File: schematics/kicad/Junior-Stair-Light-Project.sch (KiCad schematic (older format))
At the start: 107 parts, among them J1 12V Eingang, J3 CONN_01X03, J4 CONN_01X03, J5 Conn_01x10, J6 Conn_01x10, T10_1 BC337, T10_2 BC327, T11_1 BC337, T11_2 BC327, T12_1 BC337, T12_2 BC327, T13_1 BC337, T13_2 BC327, T14_1 BC337, T14_2 BC327, T15_1 BC337, T15_2 BC327, T16_1 BC337, T16_2 BC327, T17_1 BC337, T17_2 BC327, T18_1 BC337, T18_2 BC327, T19_1 BC337, T19_2 BC327, T1_1 BC337, T1_2 BC327, T2_1 BC337, T2_2 BC327, T3_1 BC337, T3_2 BC327, T4_1 BC337, T4_2 BC327, T5_1 BC337, T5_2 BC327, T6_1 BC337, T6_2 BC327, T7_1 BC337, T7_2 BC327, T8_1 BC337, T8_2 BC327, T9_1 BC337, T9_2 BC327, U1 L4940V5, U2 Arduino_Nano

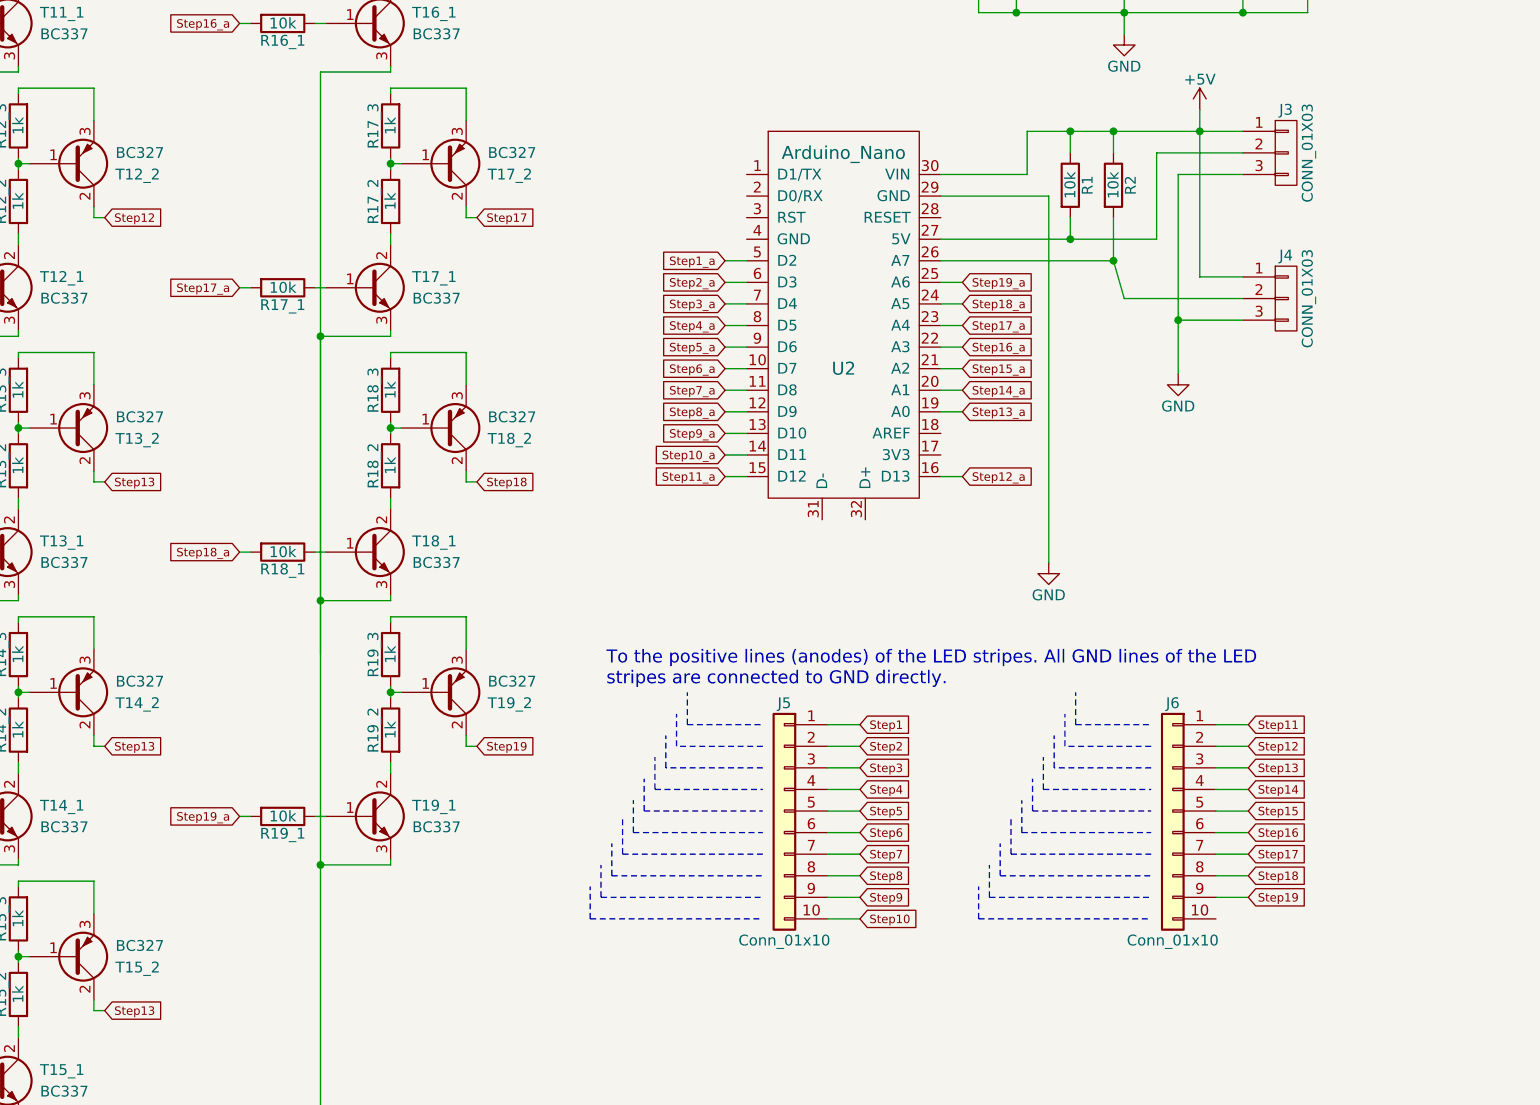
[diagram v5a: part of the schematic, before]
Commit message: Corrected connectivity, there was a bug
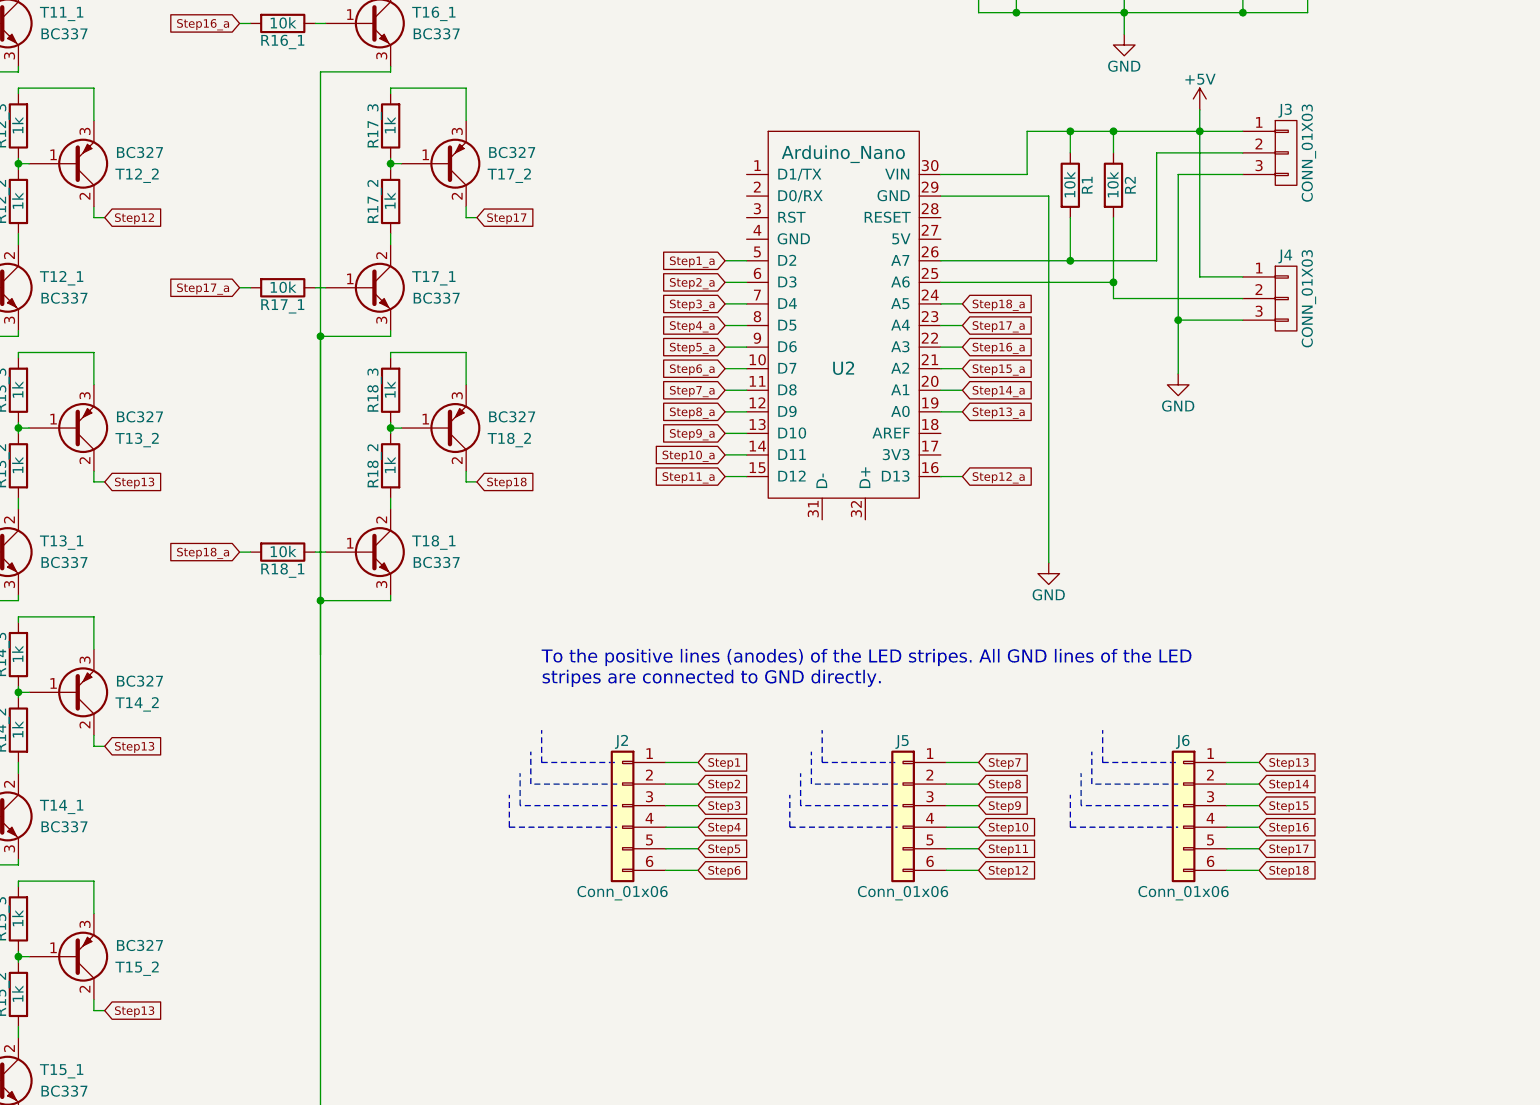
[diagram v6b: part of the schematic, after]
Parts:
- removed J5, J6: Conn_01x10, Connectors_JST:JST_XH_B10B-XH-A_10x2.50mm_Straight, symbol Conn_01x10
- removed R19_1: 10k, Resistors_THT:R_Axial_DIN0207_L6.3mm_D2.5mm_P7.62mm_Horizontal, symbol R
- removed R19_2, R19_3: 1k, Resistors_THT:R_Axial_DIN0207_L6.3mm_D2.5mm_P7.62mm_Horizontal, symbol R
- removed T19_1: BC337, TO_SOT_Packages_THT:TO-92_Inline_Narrow_Oval, symbol Q_NPN_BCE
- removed T19_2: BC327, TO_SOT_Packages_THT:TO-92_Inline_Narrow_Oval, symbol Q_PNP_BCE
- added J2, J5, J6: Conn_01x06, Connectors_JST:JST_XH_B06B-XH-A_06x2.50mm_Straight, symbol Conn_01x06
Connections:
- net Step19_a is gone; now on an unnamed net: U2.25 (A6)
- net Step1: now also J2.1 (Pin_1)
- net Step10: now also J5.4 (Pin_4)
- net Step11: now also J5.5 (Pin_5)
- net Step12: now also J5.6 (Pin_6)
- net Step13: now also J6.1 (Pin_1)
- net Step14: now also J6.2 (Pin_2)
- net Step15: now also J6.3 (Pin_3)
- net Step16: now also J6.4 (Pin_4)
- net Step17: now also J6.5 (Pin_5)
- net Step18: now also J6.6 (Pin_6)
- net Step2: now also J2.2 (Pin_2)
- net Step3: now also J2.3 (Pin_3)
- net Step4: now also J2.4 (Pin_4)
- net Step5: now also J2.5 (Pin_5)
- net Step6: now also J2.6 (Pin_6)
- net Step7: now also J5.1 (Pin_1)
- net Step8: now also J5.2 (Pin_2)
- net Step9: now also J5.3 (Pin_3)
- net at J4.2 (P2), R2.2: no longer U2.26 (A7)
- net at J3.2 (P2), R1.2: now also U2.26 (A7); no longer U2.27 (5V)

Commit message: Updates, updates, updates
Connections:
- net +5V: no longer R1.1, R2.1
- net GND: now also R1.1, R2.1
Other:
- moved on the sheet: R1, R2
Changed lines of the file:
@@
 L R R1
 U 1 1 5B89507E
-P 9825 2400
-F 0 "R1" V 9905 2400 50  0000 C CNN
-F 1 "10k" V 9825 2400 50  0000 C CNN
-F 2 "Resistors_THT:R_Axial_DIN0207_L6.3mm_D2.5mm_P7.62mm_Horizontal" V 9755 2400 50  0001 C CNN
-F 3 "" H 9825 2400 50  0001 C CNN
-	1    9825 2400
+P 9825 2550
+F 0 "R1" V 9905 2550 50  0000 C CNN
+F 1 "10k" V 9825 2550 50  0000 C CNN
+F 2 "Resistors_THT:R_Axial_DIN0207_L6.3mm_D2.5mm_P7.62mm_Horizontal" V 9755 2550 50  0001 C CNN
+F 3 "" H 9825 2550 50  0001 C CNN
+	1    9825 2550
 	1    0    0    -1
 $EndComp
@@
 	10325 2350 10325 3275
 Wire Wire Line
-	10625 2350 10325 2350
+	9825 2350 10625 2350
 Connection ~ 10325 3025
 $Comp
@@
 Connection ~ 10425 2150
 Wire Wire Line
-	10025 2550 10025 2925
+	10025 2700 10025 2925
 Wire Wire Line
 	10625 2250 10225 2250
@@
 L R R2
 U 1 1 5B89A934
-P 10025 2400
-F 0 "R2" V 10105 2400 50  0000 C CNN
-F 1 "10k" V 10025 2400 50  0000 C CNN
-F 2 "Resistors_THT:R_Axial_DIN0207_L6.3mm_D2.5mm_P7.62mm_Horizontal" V 9955 2400 50  0001 C CNN
-F 3 "" H 10025 2400 50  0001 C CNN
-	1    10025 2400
-	1    0    0    -1
-$EndComp
-Wire Wire Line
-	9825 2550 9825 2750
+P 10025 2550
+F 0 "R2" V 10105 2550 50  0000 C CNN
+F 1 "10k" V 10025 2550 50  0000 C CNN
+F 2 "Resistors_THT:R_Axial_DIN0207_L6.3mm_D2.5mm_P7.62mm_Horizontal" V 9955 2550 50  0001 C CNN
+F 3 "" H 10025 2550 50  0001 C CNN
+	1    10025 2550
+	1    0    0    -1
+$EndComp
+Wire Wire Line
+	9825 2700 9825 2750
 Connection ~ 9825 2750
 Connection ~ 10025 2850
@@
 	9400 1050 9400 1600
 Connection ~ 9575 1600
-Connection ~ 10025 2150
-Connection ~ 9825 2150
 Wire Wire Line
 	9625 2350 9625 2150
-Wire Wire Line
-	9825 2150 9825 2250
-Wire Wire Line
-	10025 2150 10025 2250
 Text GLabel 5975 1650 0    39   Input ~ 0
 Step16_a
@@
 	6675 1875 6350 1875
 Wire Wire Line
-	6350 1875 6350 4575
-Wire Wire Line
 	6675 3075 6675 3100
 Wire Wire Line
-	6675 3100 6350 3100
-Connection ~ 6350 3100
-Wire Wire Line
 	6675 4300 6675 4325
-Wire Wire Line
-	6675 4325 6350 4325
-Connection ~ 6350 4325
-Wire Wire Line
-	6350 3100 6350 6975
 Wire Wire Line
 	6350 6975 1175 6975
@@
 	-1   0    0    -1
 $EndComp
+Wire Wire Line
+	10025 2350 10025 2400
+Connection ~ 10325 2350
+Wire Wire Line
+	9825 2350 9825 2400
+Connection ~ 10025 2350
+Wire Wire Line
+	6350 1875 6350 6975
+Wire Wire Line
+	6675 3100 6350 3100
+Connection ~ 6350 3100
+Wire Wire Line
+	6675 4325 6350 4325
+Connection ~ 6350 4325
 $EndSCHEMATC
